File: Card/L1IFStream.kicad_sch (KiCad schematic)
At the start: 109 parts, among them J1 Conn_Coaxial, J2 USB_A, J3 RF_Shield_One_Piece, J4 Conn_Coaxial, U1 MAX2769BETI+T, U10 74LVC374, U11 74HC2GU04, U2 TPS717285DCK, U3 TPS717285DCK, U4 NCP164, U5 93LC66BT-I_OT, U6 FT2232H-Interface_USB, U7 74LVC1G74, U8 74LVC1G04, U9 74LVC374, X1 SIT5156, X2 SiT2024B, X3 QPQ1060

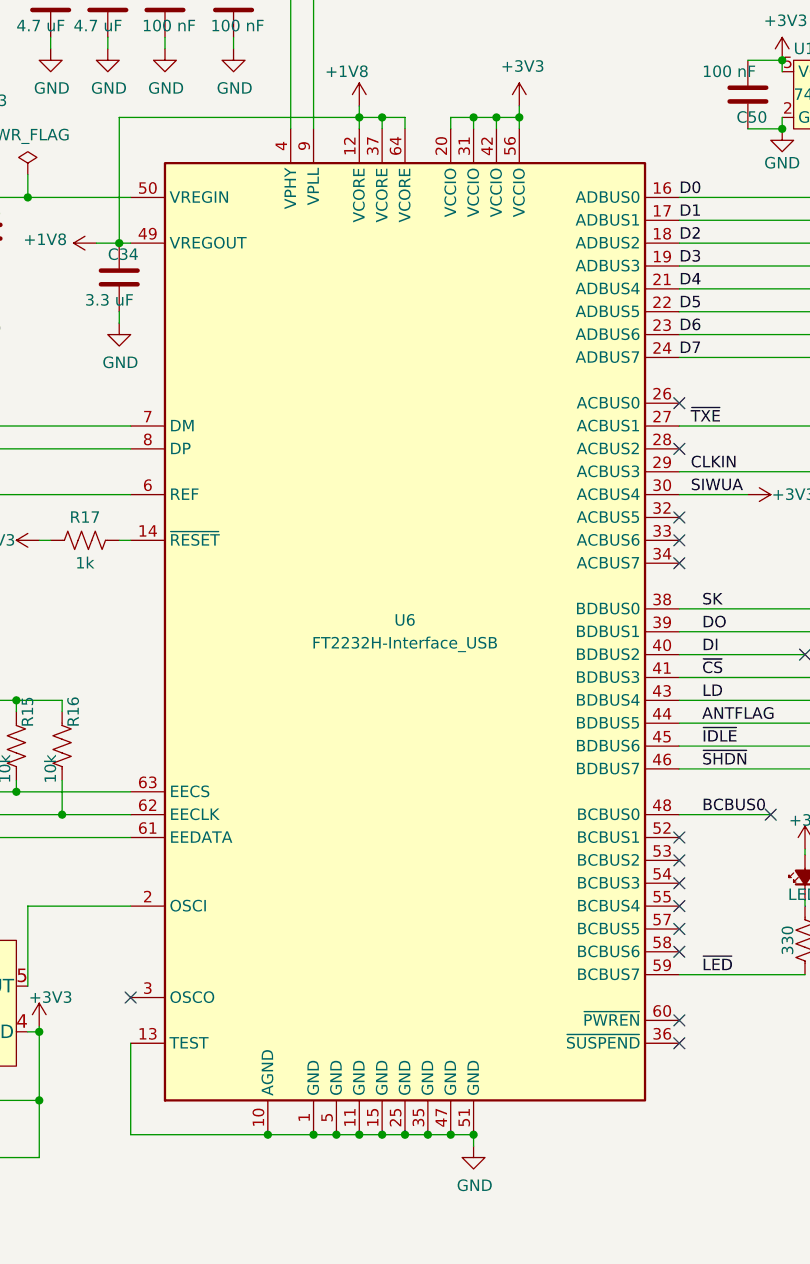
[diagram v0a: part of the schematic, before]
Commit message: Library cleaned up except for Rs and Cs
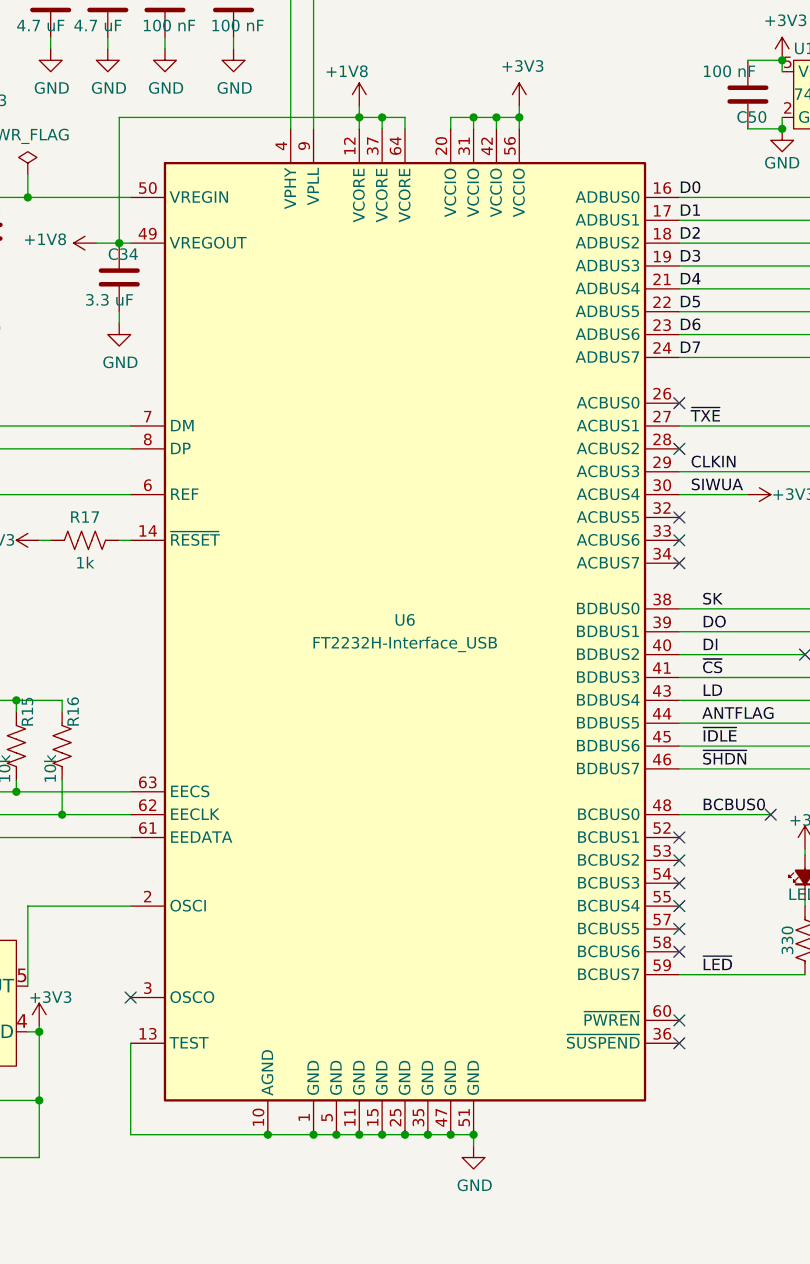
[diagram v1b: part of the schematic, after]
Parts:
- D1: footprint L1IFStream:LED_0603_1608Metric -> L1IF:LED_0603_1608Metric; symbol L1IFStream:LED_Small_Filled -> L1IF:LED_0603; Digi-Key QBLP601-AG1-2943 -> (none); Manufacturer (none) -> QT Brightek (QTB); Vendor (none) -> DigiKey; Vendor PN (none) -> 1516-QBLP601-AG1-2943DKR-ND
- D2: footprint L1IFStream:Texas_DPY0002A_0.6x1mm_P0.65mm -> L1IF:Texas_DPY0002A_0.6x1mm_P0.65mm; symbol L1IFStream:TPD1E10B06 -> L1IF:TPD1E10B06; Digi-Key 296-TPD1E10B06QDPYRQ1DKR-ND -> (none); Manufacturer (none) -> Texas Instruments; Vendor (none) -> DigiKey; Vendor PN (none) -> 296-TPD1E10B06QDPYRQ1DKR-ND
- D3, D4: footprint L1IFStream:DPY-PX1SON_1.0mmx0.6mm -> L1IF:Texas_DPY0002A_0.6x1mm_P0.65mm; symbol L1IFStream:ESD321 -> L1IF:ESD321; Digi-Key 296-51108-6-ND -> (none); Manufacturer (none) -> Texas Instruments; Vendor (none) -> DigiKey; Vendor PN (none) -> 296-51108-6-ND
- D5, D6: footprint L1IFStream:Texas_DPY0002A_0.6x1mm_P0.65mm -> L1IF:Texas_DPY0002A_0.6x1mm_P0.65mm; symbol L1IFStream:TPD1E01B04 -> L1IF:TPD1E01B04; Digi-Key 296-TPD1E01B04DPYRQ1DKR-ND -> (none); Manufacturer (none) -> Texas Instruments; Vendor (none) -> DigiKey; Vendor PN (none) -> 296-TPD1E01B04DPYRQ1DKR-ND
- FB1, FB2: footprint L1IFStream:C_0805_2012Metric -> L1IF:C_0805_2012Metric; symbol L1IFStream-rescue:Ferrite_Bead-MAX2769FT2232H -> L1IF:Ferrite_Bead; Digi-Key 490-1041-1-ND -> (none); MPN (none) -> BLM21AG102SN1D; Manufacturer (none) -> Murata Electronics; Vendor (none) -> DigiKey; Vendor PN (none) -> 490-1041-6-ND
- H1, H2, H3, H4: footprint L1IFStream:MountingHole_2.2mm_M2_Pad_Via -> L1IF:MountingHole_2.2mm_M2_Pad_Via; symbol L1IFStream-rescue:MountingHole_Pad-MAX2769FT2232H -> L1IF:MountingHole_Pad
- J1: footprint L1IFStream:SMA_Amphenol_132203-12_Horizontal -> L1IF:SMA_Amphenol_132203-12_Horizontal; symbol L1IFStream-rescue:Conn_Coaxial-MAX2769FT2232H -> L1IF:Conn_Coaxial; Digi-Key ACX1232-ND -> (none); MPN (none) -> 132136; Manufacturer (none) -> Amphenol RF; Vendor (none) -> DigiKey; Vendor PN (none) -> ACX1232-ND
- J2: footprint L1IFStream:USB_A_CNCTech_1001-011-01101_Horizontal -> L1IF:USB_A_CNCTech_1001-011-01101_Horizontal; symbol L1IFStream-rescue:USB_A-MAX2769FT2232H -> L1IF:USB_A; Digi-Key WM3983CT-ND -> (none); MPN (none) -> 0480372200; Manufacturer (none) -> Molex; Vendor (none) -> DigiKey; Vendor PN (none) -> WM3983DKR-ND
- J3: footprint L1IFStream:Laird_Technologies_BMI-S-103_26.21x26.21mm -> L1IF:Laird_Technologies_BMI-S-103_26.21x26.21mm; symbol L1IFStream-rescue:RF_Shield_One_Piece-MAX2769FT2232H -> L1IF:RF_Shield_One_Piece; Digi-Key 903-1008-1-ND -> (none); MPN (none) -> BMI-S-103; Manufacturer (none) -> Laird Technologies EMI; Vendor (none) -> DigiKey; Vendor PN (none) -> 903-1008-6-ND
- J4: footprint L1IFStream:MMCX_Molex_73415-1471_Vertical -> L1IF:MMCX_Molex_73415-1471_Vertical; symbol L1IFStream-rescue:Conn_Coaxial-MAX2769FT2232H -> L1IF:Conn_Coaxial; Digi-Key ARF1904-ND -> (none); MPN (none) -> 908-22106; Manufacturer (none) -> Amphenol RF; Vendor (none) -> DigiKey; Vendor PN (none) -> ARF1904-ND
- L1: footprint L1IFStream:L_0402_1005Metric -> L1IF:L_0402_1005Metric; symbol L1IFStream-rescue:L-MAX2769FT2232H -> L1IF:Inductor; Digi-Key 490-2629-1-ND -> (none); MPN (none) -> LQG15HS33NJ02D; Manufacturer (none) -> Murata Electronics; Vendor (none) -> DigiKey; Vendor PN (none) -> 490-2629-6-ND
- TP1, TP2, TP3, TP4: footprint L1IFStream:TestPoint_Pad_D1.0mm -> L1IF:TestPoint_Pad_D1.0mm; symbol Connector:TestPoint -> L1IF:TestPoint
- U10, U9: footprint L1IFStream:TSSOP-20_4.4x6.5mm_P0.65mm -> L1IF:TSSOP-20_4.4x6.5mm_P0.65mm; symbol L1IFStream-rescue:74LVC374-MAX2769FT2232H -> L1IF:74LVC374; DS1 (none) -> https://assets.nexperia.com/documents/data-sheet/74LVC374A.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; Manufacturer Nexperia -> Nexperia USA Inc.; Vendor P/N# 1727-4034-1-ND -> (none); Vendor PN (none) -> 1727-4034-1-ND
- U11: footprint L1IFStream:SOT-363_SC-70-6 -> L1IF:SOT-363_SC-70-6; symbol L1IFStream:74HC2UG04 -> L1IF:74HC2GU04; MPN 74HC2G04GW,125 -> 74HC2GU04GW,125; Vendor P/N# 1727-6045-1-ND -> (none); Vendor PN (none) -> 1727-6915-6-ND
- U5: footprint L1IFStream:93LC66BT-I&slash_OT -> L1IF:SOT-23-6; symbol L1IFStream-rescue:93LC66BT-I_OT-MAX2769FT2232H -> L1IF:93LC66BT-I_OT; Vendor P/N# 93LC66BT-I/OTCT-ND -> (none); Vendor PN (none) -> 93LC66BT-I/OTCT-ND
- U6: footprint L1IFStream:LQFP-64_10x10mm_P0.5mm -> L1IF:LQFP-64_10x10mm_P0.5mm; symbol L1IFStream-rescue:FT2232H-Interface_USB-MAX2769FT2232H -> L1IF:FT2232HL; Vendor P/N# 768-1024-1-ND -> (none); Vendor PN (none) -> 768-1024-6-ND
- U7: footprint L1IFStream:SOT-833-1 -> L1IF:SOT-833-1; symbol L1IFStream-rescue:74LVC1G74-MAX2769FT2232H -> L1IF:74LVC1G74; Manufacturer Nexperia -> Nexperia USA Inc.; Notes (none) -> http://www.ti.com/lit/sg/scyt129e/scyt129e.pdf; Vendor P/N# 1727-3558-1-ND -> (none); Vendor PN (none) -> 1727-3558-6-ND
- U8: footprint L1IFStream:SOT-353_SC-70-5 -> L1IF:SOT-353_SC-70-5; symbol L1IFStream:74LVC1G04 -> L1IF:74LVC1G04; Vendor P/N# 1727-2871-1-ND -> (none); Vendor PN (none) -> 1727-2871-1-ND

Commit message: Library cleanup capacitors
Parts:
- C1: footprint L1IFStream:C_0402_1005Metric -> L1IF:C_0402_1005Metric; symbol L1IFStream-rescue:C-MAX2769FT2232H -> L1IF:Capacitor; Digi-Key 490-12651-1-ND -> (none); MPN (none) -> GCM1555C1H270JA16D; Manufacturer (none) -> Murata Electronics; Vendor (none) -> DigiKey; Vendor PN (none) -> 490-12651-1-ND
- C2, C46, C9: footprint L1IFStream:C_0402_1005Metric -> L1IF:C_0402_1005Metric; symbol L1IFStream-rescue:C-MAX2769FT2232H -> L1IF:Capacitor; Digi-Key 490-6242-1-ND -> (none); MPN (none) -> GRM1555C1H471JA01J; Manufacturer (none) -> Murata Electronics; Vendor (none) -> DigiKey; Vendor PN (none) -> 490-6242-6-ND
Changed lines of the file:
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@@
     )
   )
-  (symbol (lib_id "L1IFStream-rescue:C-MAX2769FT2232H") (at 346.71 24.13 0) (unit 1)
+  (symbol (lib_id "L1IF:Capacitor") (at 346.71 24.13 0) (unit 1)
     (in_bom yes) (on_board yes) (dnp no)
     (property "Reference" "C9" (at 345.44 21.59 0)
@@
       (effects (font (size 1.27 1.27)) (justify left))
     )
-    (property "Footprint" "L1IFStream:C_0402_1005Metric" (at 347.6752 27.94 0)
+    (property "Footprint" "L1IF:C_0402_1005Metric" (at 347.6752 27.94 0)
       (effects (font (size 1.27 1.27)) hide)
     )
@@
       (effects (font (size 1.27 1.27)) hide)
     )
-    (property "Digi-Key" "490-6242-1-ND" (at 346.71 24.13 0)
+    (property "Manufacturer" "Murata Electronics" (at 346.71 24.13 0)
+      (effects (font (size 1.27 1.27)) hide)
+    )
+    (property "MPN" "GRM1555C1H471JA01J" (at 346.71 24.13 0)
+      (effects (font (size 1.27 1.27)) hide)
+    )
+    (property "Vendor" "DigiKey" (at 346.71 24.13 0)
+      (effects (font (size 1.27 1.27)) hide)
+    )
+    (property "Vendor PN" "490-6242-6-ND" (at 346.71 24.13 0)
       (effects (font (size 1.27 1.27)) hide)
     )
@@
     )
   )
-  (symbol (lib_id "L1IFStream-rescue:C-MAX2769FT2232H") (at 394.97 17.78 0) (unit 1)
+  (symbol (lib_id "L1IF:Capacitor") (at 394.97 17.78 0) (unit 1)
     (in_bom yes) (on_board yes) (dnp no)
     (property "Reference" "C46" (at 394.97 15.24 0)
@@
       (effects (font (size 1.27 1.27)) (justify left))
     )
-    (property "Footprint" "L1IFStream:C_0402_1005Metric" (at 395.9352 21.59 0)
+    (property "Footprint" "L1IF:C_0402_1005Metric" (at 395.9352 21.59 0)
       (effects (font (size 1.27 1.27)) hide)
     )
@@
       (effects (font (size 1.27 1.27)) hide)
     )
-    (property "Digi-Key" "490-6242-1-ND" (at 394.97 17.78 0)
+    (property "Manufacturer" "Murata Electronics" (at 394.97 17.78 0)
+      (effects (font (size 1.27 1.27)) hide)
+    )
+    (property "MPN" "GRM1555C1H471JA01J" (at 394.97 17.78 0)
+      (effects (font (size 1.27 1.27)) hide)
+    )
+    (property "Vendor" "DigiKey" (at 394.97 17.78 0)
+      (effects (font (size 1.27 1.27)) hide)
+    )
+    (property "Vendor PN" "490-6242-6-ND" (at 394.97 17.78 0)
       (effects (font (size 1.27 1.27)) hide)
     )
@@
     )
   )
-  (symbol (lib_id "L1IFStream-rescue:C-MAX2769FT2232H") (at 335.915 92.075 90) (mirror x) (unit 1)
+  (symbol (lib_id "L1IF:Capacitor") (at 335.915 92.075 90) (mirror x) (unit 1)
     (in_bom yes) (on_board yes) (dnp no)
     (property "Reference" "C2" (at 334.645 93.345 90)
@@
       (effects (font (size 1.27 1.27)) (justify left))
     )
-    (property "Footprint" "L1IFStream:C_0402_1005Metric" (at 339.725 93.0402 0)
+    (property "Footprint" "L1IF:C_0402_1005Metric" (at 339.725 93.0402 0)
       (effects (font (size 1.27 1.27)) hide)
     )
@@
       (effects (font (size 1.27 1.27)) hide)
     )
-    (property "Digi-Key" "490-6242-1-ND" (at 335.915 92.075 0)
+    (property "Manufacturer" "Murata Electronics" (at 335.915 92.075 0)
+      (effects (font (size 1.27 1.27)) hide)
+    )
+    (property "MPN" "GRM1555C1H471JA01J" (at 335.915 92.075 0)
+      (effects (font (size 1.27 1.27)) hide)
+    )
+    (property "Vendor" "DigiKey" (at 335.915 92.075 0)
+      (effects (font (size 1.27 1.27)) hide)
+    )
+    (property "Vendor PN" "490-6242-6-ND" (at 335.915 92.075 0)
       (effects (font (size 1.27 1.27)) hide)
     )
@@
     )
   )
-  (symbol (lib_id "L1IFStream-rescue:C-MAX2769FT2232H") (at 335.915 83.82 90) (mirror x) (unit 1)
+  (symbol (lib_id "L1IF:Capacitor") (at 335.915 83.82 90) (mirror x) (unit 1)
     (in_bom yes) (on_board yes) (dnp no)
     (property "Reference" "C1" (at 335.28 85.09 90)
@@
       (effects (font (size 1.27 1.27)) (justify left))
     )
-    (property "Footprint" "L1IFStream:C_0402_1005Metric" (at 339.725 84.7852 0)
+    (property "Footprint" "L1IF:C_0402_1005Metric" (at 339.725 84.7852 0)
       (effects (font (size 1.27 1.27)) hide)
     )
@@
       (effects (font (size 1.27 1.27)) hide)
     )
-    (property "Digi-Key" "490-12651-1-ND" (at 335.915 83.82 0)
+    (property "Manufacturer" "Murata Electronics" (at 335.915 83.82 0)
+      (effects (font (size 1.27 1.27)) hide)
+    )
+    (property "MPN" "GCM1555C1H270JA16D" (at 335.915 83.82 0)
+      (effects (font (size 1.27 1.27)) hide)
+    )
+    (property "Vendor" "DigiKey" (at 335.915 83.82 0)
+      (effects (font (size 1.27 1.27)) hide)
+    )
+    (property "Vendor PN" "490-12651-1-ND" (at 335.915 83.82 0)
       (effects (font (size 1.27 1.27)) hide)
     )

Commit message: Library cleaned up through resistors. Just caps to go.
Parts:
- R1: footprint L1IFStream:R_0603_1608Metric -> L1IF:R_0603_1608Metric; symbol L1IFStream-rescue:R_US-MAX2769FT2232H -> L1IF:Resistor; Digi-Key 2019-RK73H1JTTD2002FCT-ND -> (none); MPN (none) -> RK73H1JTTD2002F; Manufacturer (none) -> KOA Speer Electronics, Inc.; Vendor (none) -> DigiKey; Vendor PN (none) -> 2019-RK73H1JTTD2002FDKR-ND
- R10, R11, R2, R20, R21, R3, R4, R5, R6, R7, R8, R9: footprint L1IFStream:R_0603_1608Metric -> L1IF:R_0603_1608Metric; symbol L1IFStream-rescue:R_US-MAX2769FT2232H -> L1IF:Resistor; Digi-Key 2019-RK73Z1JTTDCT-ND -> (none); MPN (none) -> RK73Z1JTTD; Manufacturer (none) -> KOA Speer Electronics, Inc.; Vendor (none) -> DigiKey; Vendor PN (none) -> 2019-RK73Z1JTTDDKR-ND
- R12: footprint L1IFStream:R_0603_1608Metric -> L1IF:R_0603_1608Metric; symbol L1IFStream-rescue:R_US-MAX2769FT2232H -> L1IF:Resistor; Digi-Key 2019-RK73H1JTTD2201FCT-ND -> (none); MPN (none) -> RK73H1JTTD2201F; Manufacturer (none) -> KOA Speer Electronics, Inc.; Vendor (none) -> DigiKey; Vendor PN (none) -> 2019-RK73H1JTTD2201FDKR-ND
- R13: footprint L1IFStream:R_0603_1608Metric -> L1IF:R_0603_1608Metric; symbol Device:R_US -> L1IF:Resistor; Digi-Key 2019-RK73H1JTTD1001FCT-ND -> (none); MPN (none) -> RK73H1JTTD1001F; Manufacturer (none) -> KOA Speer Electronics, Inc.; Vendor (none) -> DigiKey; Vendor PN (none) -> 2019-RK73H1JTTD1001FDKR-ND
- R14: footprint L1IFStream:R_0603_1608Metric -> L1IF:R_0603_1608Metric; symbol L1IFStream-rescue:R_US-MAX2769FT2232H -> L1IF:Resistor; MPN (none) -> RK73H1JTTD1202F; Manufacturer (none) -> KOA Speer Electronics, Inc.; Vendor (none) -> DigiKey; Vendor PN (none) -> 2019-RK73H1JTTD1202FDKR-ND
- R15, R16, R18: footprint L1IFStream:R_0603_1608Metric -> L1IF:R_0603_1608Metric; symbol L1IFStream-rescue:R_US-MAX2769FT2232H -> L1IF:Resistor; Digi-Key 2019-RK73H1JTTD1002FCT-ND -> (none); MPN (none) -> RK73H1JTTD1002F; Manufacturer (none) -> KOA Speer Electronics, Inc.; Vendor (none) -> DigiKey; Vendor PN (none) -> 2019-RK73H1JTTD1002FDKR-ND
- R17: footprint L1IFStream:R_0603_1608Metric -> L1IF:R_0603_1608Metric; symbol L1IFStream-rescue:R_US-MAX2769FT2232H -> L1IF:Resistor; Digi-Key 2019-RK73H1JTTD1001FCT-ND -> (none); MPN (none) -> RK73H1JTTD1001F; Manufacturer (none) -> KOA Speer Electronics, Inc.; Vendor (none) -> DigiKey; Vendor PN (none) -> 2019-RK73H1JTTD1001FDKR-ND
- R19: footprint L1IFStream:R_0603_1608Metric -> L1IF:R_0603_1608Metric; symbol L1IFStream-rescue:R_US-MAX2769FT2232H -> L1IF:Resistor; Digi-Key 2019-RK73H1JTTD3300FDKR-ND -> (none); Manufacturer (none) -> KOA Speer Electronics, Inc.; Vendor (none) -> DigiKey; Vendor PN (none) -> 2019-RK73H1JTTD3300FDKR-ND

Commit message: Library Cleaned Up
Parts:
- C10, C11, C47, C48: footprint L1IFStream:C_0402_1005Metric -> L1IF:C_0402_1005Metric; symbol L1IFStream-rescue:C-MAX2769FT2232H -> L1IF:Capacitor; Digi-Key 399-7759-1-ND -> (none); MPN (none) -> C0402C103K8RAC7867; Manufacturer (none) -> KEMET; Vendor (none) -> DigiKey; Vendor PN (none) -> 399-C0402C103K8RAC7867DKR-ND
- C12: footprint L1IFStream:C_0402_1005Metric -> L1IF:C_0402_1005Metric; symbol L1IFStream-rescue:C-MAX2769FT2232H -> L1IF:Capacitor; DNP (none) -> DNP; Digi-Key 490-6242-1-ND -> (none); MPN (none) -> GRM1555C1H471JA01J; Manufacturer (none) -> Murata Electronics; Vendor (none) -> DigiKey; Vendor PN (none) -> 490-6242-6-ND
- C13, C14, C15, C16, C17, C18, C19: footprint L1IFStream:C_0402_1005Metric -> L1IF:C_0402_1005Metric; symbol L1IFStream-rescue:C-MAX2769FT2232H -> L1IF:Capacitor; Digi-Key 399-3194-1-ND -> (none); MPN (none) -> C0402C101J5GAC7867; Manufacturer (none) -> KEMET; Vendor (none) -> DigiKey; Vendor PN (none) -> 399-C0402C101J5GAC7867DKR-ND
- C20, C23, C27, C29, C3, C35, C36, C37, C38, C39, C4, C40, C41, C42, C43, C44, C45, C49, C5, C50, C51, C52, C53, C6, C7, C8: footprint L1IFStream:C_0402_1005Metric -> L1IF:C_0402_1005Metric; symbol L1IFStream-rescue:C-MAX2769FT2232H -> L1IF:Capacitor; Digi-Key 490-6328-1-ND -> (none); MPN (none) -> GRM155R71C104KA88J; Manufacturer (none) -> Murata Electronics; Vendor (none) -> DigiKey; Vendor PN (none) -> 490-6328-6-ND
- C21, C24, C25, C28, C30, C31: footprint L1IFStream:C_0402_1005Metric -> L1IF:C_0402_1005Metric; symbol L1IFStream-rescue:C-MAX2769FT2232H -> L1IF:Capacitor; Digi-Key 490-12233-1-ND -> (none); MPN (none) -> GRT155C80J105KE01D; Manufacturer (none) -> Murata Electronics; Vendor (none) -> DigiKey; Vendor PN (none) -> 490-12233-6-ND
- C22, C26: footprint L1IFStream:C_0402_1005Metric -> L1IF:C_0402_1005Metric; symbol L1IFStream-rescue:C-MAX2769FT2232H -> L1IF:Capacitor; DNP (none) -> DNP; Digi-Key 399-7759-1-ND -> (none); MPN (none) -> C0402C103K8RAC7867; Manufacturer (none) -> KEMET; Vendor (none) -> DigiKey; Vendor PN (none) -> 399-C0402C103K8RAC7867DKR-ND
- C32, C33: footprint L1IFStream:C_0805_2012Metric -> L1IF:C_0805_2012Metric; symbol L1IFStream-rescue:C-MAX2769FT2232H -> L1IF:Capacitor; Digi-Key 399-15725-1-ND -> (none); MPN (none) -> C0805C475J9RACAUTO; Manufacturer (none) -> KEMET; Vendor (none) -> DigiKey; Vendor PN (none) -> 399-15725-6-ND
- C34: footprint L1IFStream:C_0805_2012Metric -> L1IF:C_0805_2012Metric; symbol L1IFStream-rescue:C-MAX2769FT2232H -> L1IF:Capacitor; Digi-Key 490-13309-1-ND -> (none); MPN (none) -> GCM21BR71C335KA73L; Manufacturer (none) -> Murata Electronics; Vendor (none) -> DigiKey; Vendor PN (none) -> 490-13309-6-ND
- R10, R20, R3, R6, R8, R9: DNP (none) -> DNP
- R14: Digi-Key 2019-RK73H1JTTD1202FCT-ND -> (none)
